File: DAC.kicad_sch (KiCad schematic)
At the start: 7 parts

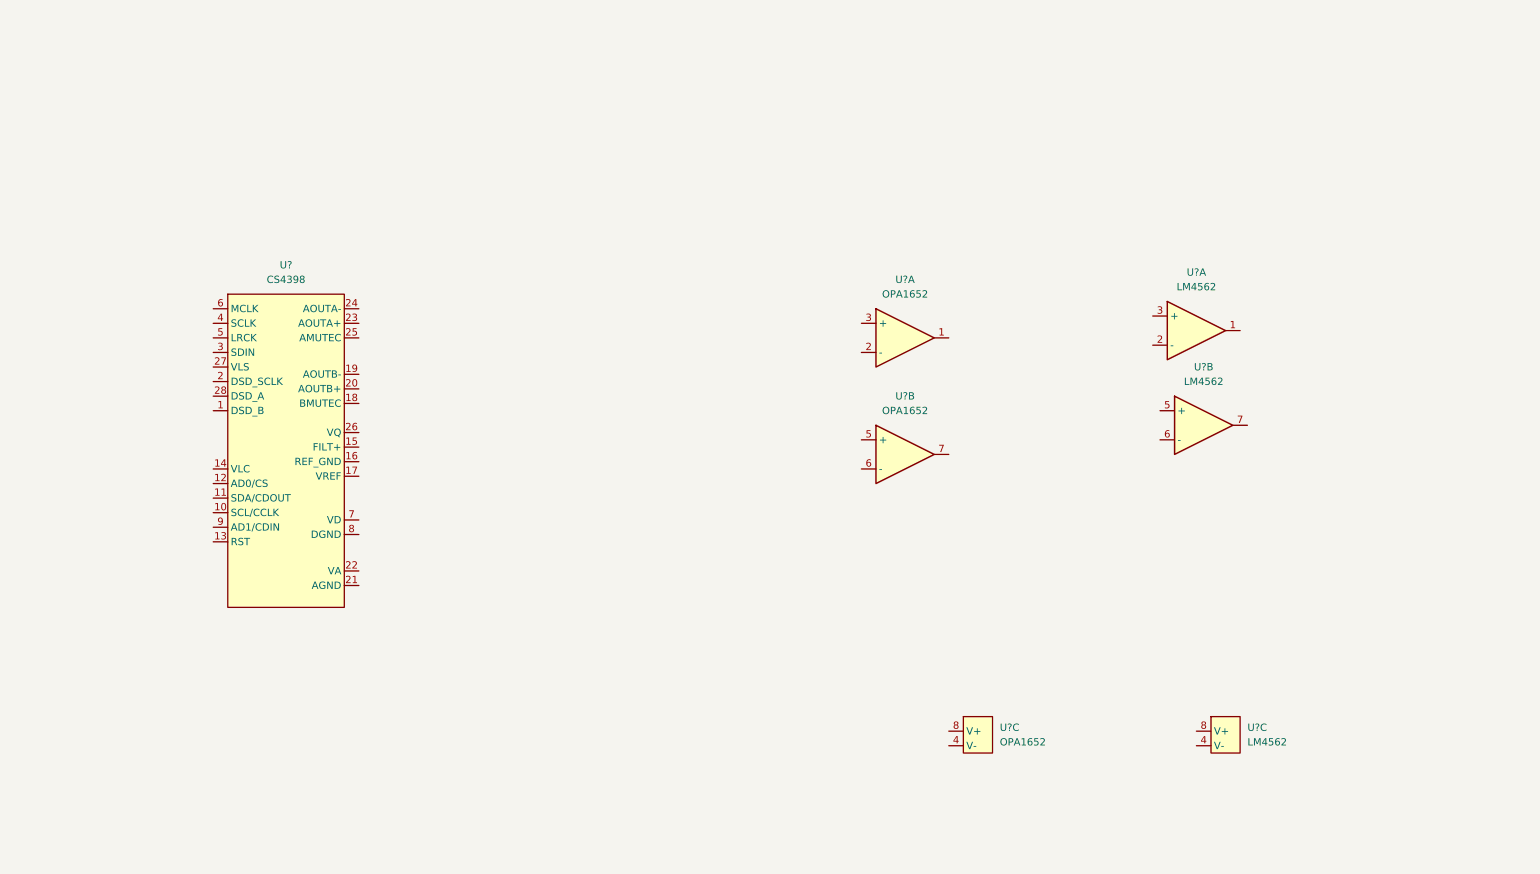
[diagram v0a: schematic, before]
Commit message: added SOC list
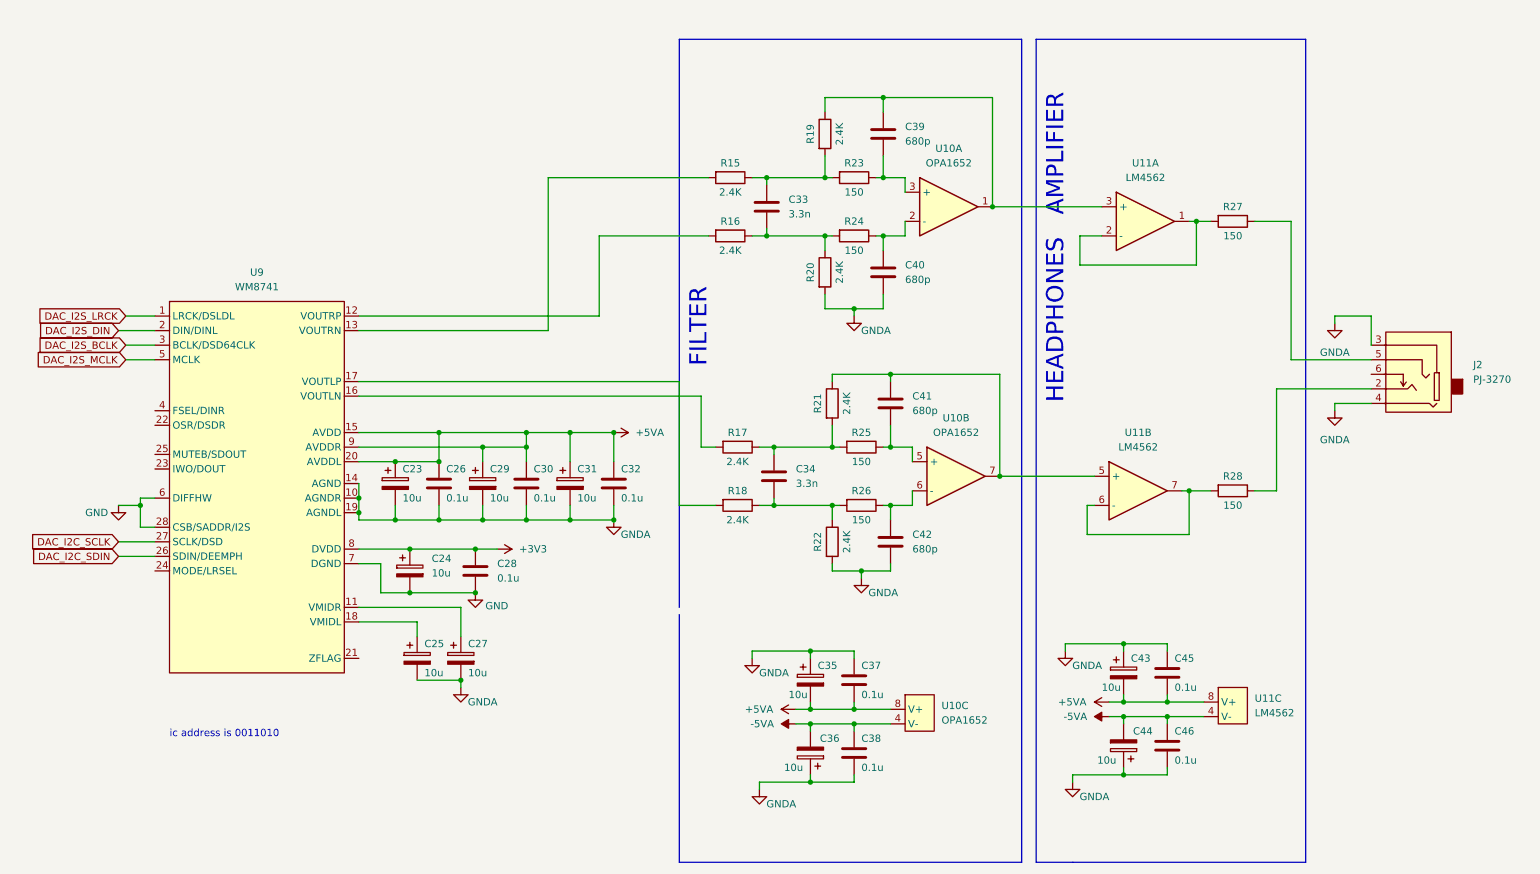
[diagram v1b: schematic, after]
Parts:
- removed U?: CS4398, Package_SO:TSSOP-28_6.1x9.7mm_P0.65mm, symbol rlib_ic:CS4398
- added C23, C24, C25, C27, C29, C31, C35, C36, C43, C44: 10u, symbol Device:C_Polarized
- added C26, C28, C30, C32, C37, C38, C45, C46: 0.1u, symbol Device:C
- added C33, C34: 3.3n, symbol Device:C
- added C39, C40, C41, C42: 680p, symbol Device:C
- added J2: PJ-3270, rlib_connectors:PJ-3270, symbol rlib_connectors:PJ-3270
- added R15, R16, R17, R18, R19, R20, R21, R22: 2.4K, symbol Device:R
- added R23, R24, R25, R26, R27, R28: 150, symbol Device:R
- added U9: WM8741, Package_SO:SSOP-28_5.3x10.2mm_P0.65mm, symbol rlib_ic:WM8741
- gave numbers to parts that had none: 2
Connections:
- net at U11.1: now also U11.2 (-), R27.2
- net at U11.3 (+): now also U10.1, C39.1, R19.1
- net at U10.2 (-): now also C40.1, R24.1
- net at U10.3 (+): now also C39.2, R23.1
- net at U10.5 (+): now also C41.2, R25.1
- net at U10.6 (-): now also C42.1, R26.1
- net at U10.7: now also U11.5 (+), C41.1, R21.1
- net -5VA: now reaches U10.4 (V-)
- net -5VA: now also U11.4 (V-), C36.2, C38.1, C44.2, C46.1
- net +5VA: now reaches U10.8 (V+)
- net +5VA: now also U11.8 (V+), C23.1, C26.1, C29.1, C30.1, C31.1, C32.1, C35.2, C37.2, C43.2, C45.2, U9.15 (AVDD), U9.20 (AVDDL), U9.9 (AVDDR)
- net at U11.6 (-): now also U11.7, R28.2
- new net: C34.1, R17.1, R21.2, R25.2
- new net: C34.2, R18.1, R22.1, R26.2
- new net: R17.2, U9.16 (VOUTLN)
- new net: J2.5, R27.1
- new net: J2.2, R28.1
- new net: C33.2, R16.1, R20.1, R24.2
- new net: C33.1, R15.1, R19.2, R23.2
- new net: C27.1, U9.11 (VMIDR)
- new net: R16.2, U9.12 (VOUTRP)
- new net: R15.2, U9.13 (VOUTRN)
- new net: R18.2, U9.17 (VOUTLP)
- new net: C25.1, U9.18 (VMIDL)
- new net +3V3: C24.1, C28.1, U9.8 (DVDD)
- new net DAC_I2C_SCLK: U9.27 (SCLK/DSD)
- new net DAC_I2C_SDIN: U9.26 (SDIN/DEEMPH)
- new net DAC_I2S_BCLK: U9.3 (BCLK/DSD64CLK)
- new net DAC_I2S_DIN: U9.2 (DIN/DINL)
- new net DAC_I2S_LRCK: U9.1 (LRCK/DSLDL)
- new net DAC_I2S_MCLK: U9.5 (MCLK)
- new net GND: C24.2, C28.2, U9.28 (CSB/SADDR/I2S), U9.6 (DIFFHW), U9.7 (DGND)
- new net GNDA: C23.2, C25.2, C26.2, C27.2, C29.2, C30.2, C31.2, C32.2, C35.1, C36.1, C37.1, C38.2, C40.2, C42.2, C43.1, C44.1, C45.1, C46.2, J2.3, J2.4, R20.2, R22.2, U9.10 (AGNDR), U9.14 (AGND), U9.19 (AGNDL)
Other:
- note added: "FILTER"
- note added: "HEADPHONES AMPLIFIER"
- note added: "ic address is 0011010"
- moved on the sheet: U10A, U10B, U10C, U11A, U11B, U11C

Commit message: dfdfasfasf
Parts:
- C23, C24, C25, C27, C29, C31, C35, C36, C43, C44: symbol Device:C_Polarized -> rlib_passive:C_Pol
- C26, C28, C30, C32, C33, C34, C37, C38, C39, C40, C41, C42, C45, C46: symbol Device:C -> rlib_passive:C
- R15, R16, R17, R18, R19, R20, R21, R22, R23, R24, R25, R26, R27, R28: symbol Device:R -> rlib_passive:R
- U10, U11: footprint Package_SO:SOIC-8_3.9x4.9mm_P1.27mm -> rlib_ic:SOIC-8_3.9x4.9mm_P1.27mm
- U9: footprint Package_SO:SSOP-28_5.3x10.2mm_P0.65mm -> rlib_ic:SSOP-28_5.3x10.2mm_P0.65mm

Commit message: lradc schematic
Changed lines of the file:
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@@
     (stroke (width 0) (type default) (color 0 0 0 1))
   )
-  (text "ic address is 0011010 " (at 38.1 137.16 0)
+  (text "ic address is 0011010 " (at 38.1 129.54 0)
     (effects (font (size 1.27 1.27)) (justify left bottom))
   )

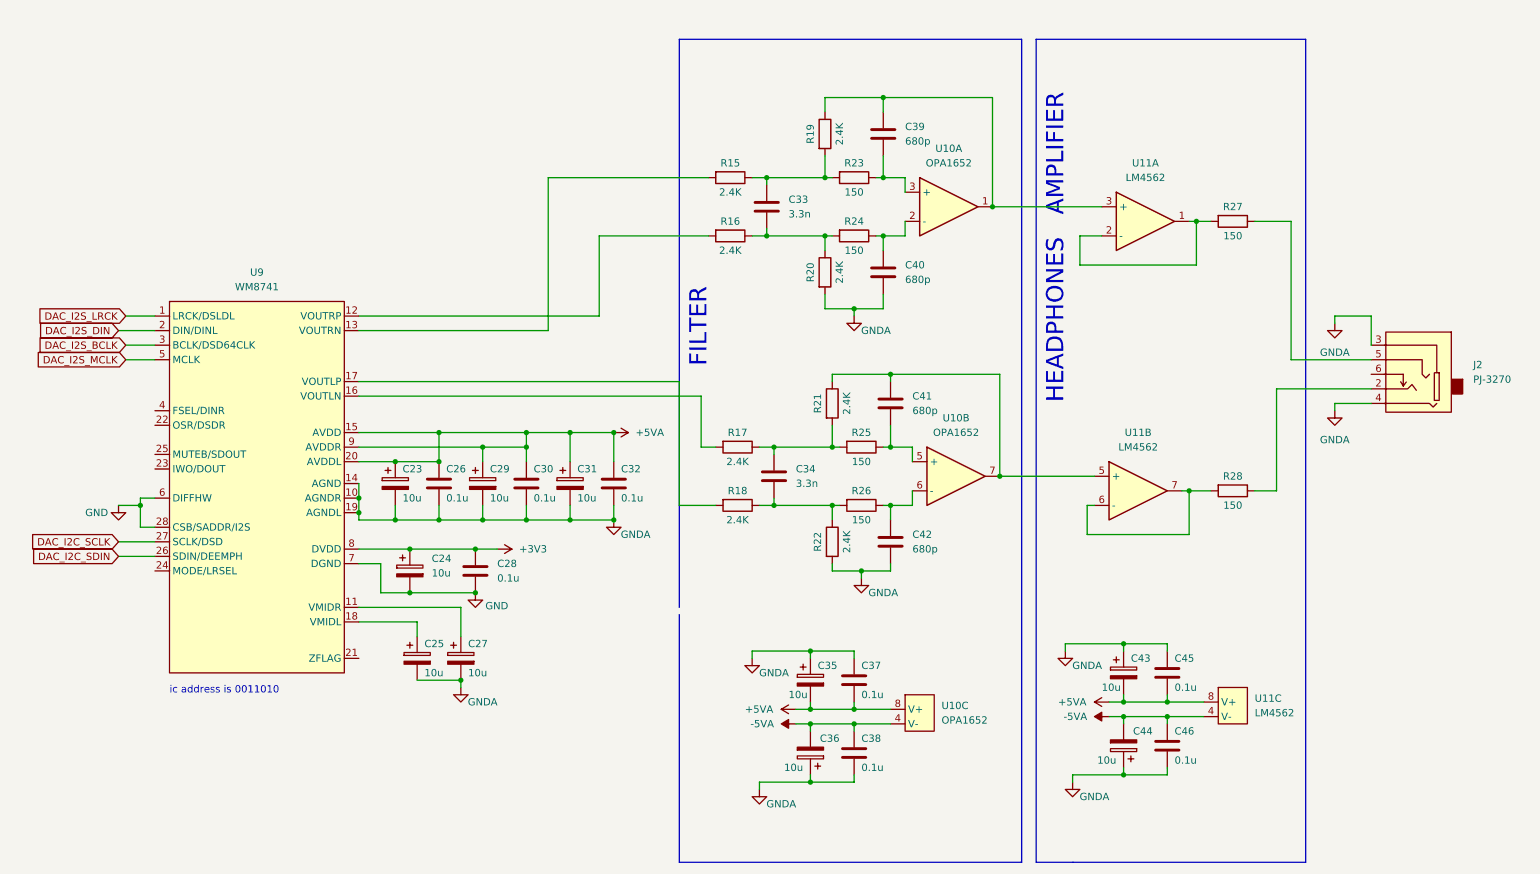
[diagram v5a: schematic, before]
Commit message: added crystal,backlight regulator and usb nets
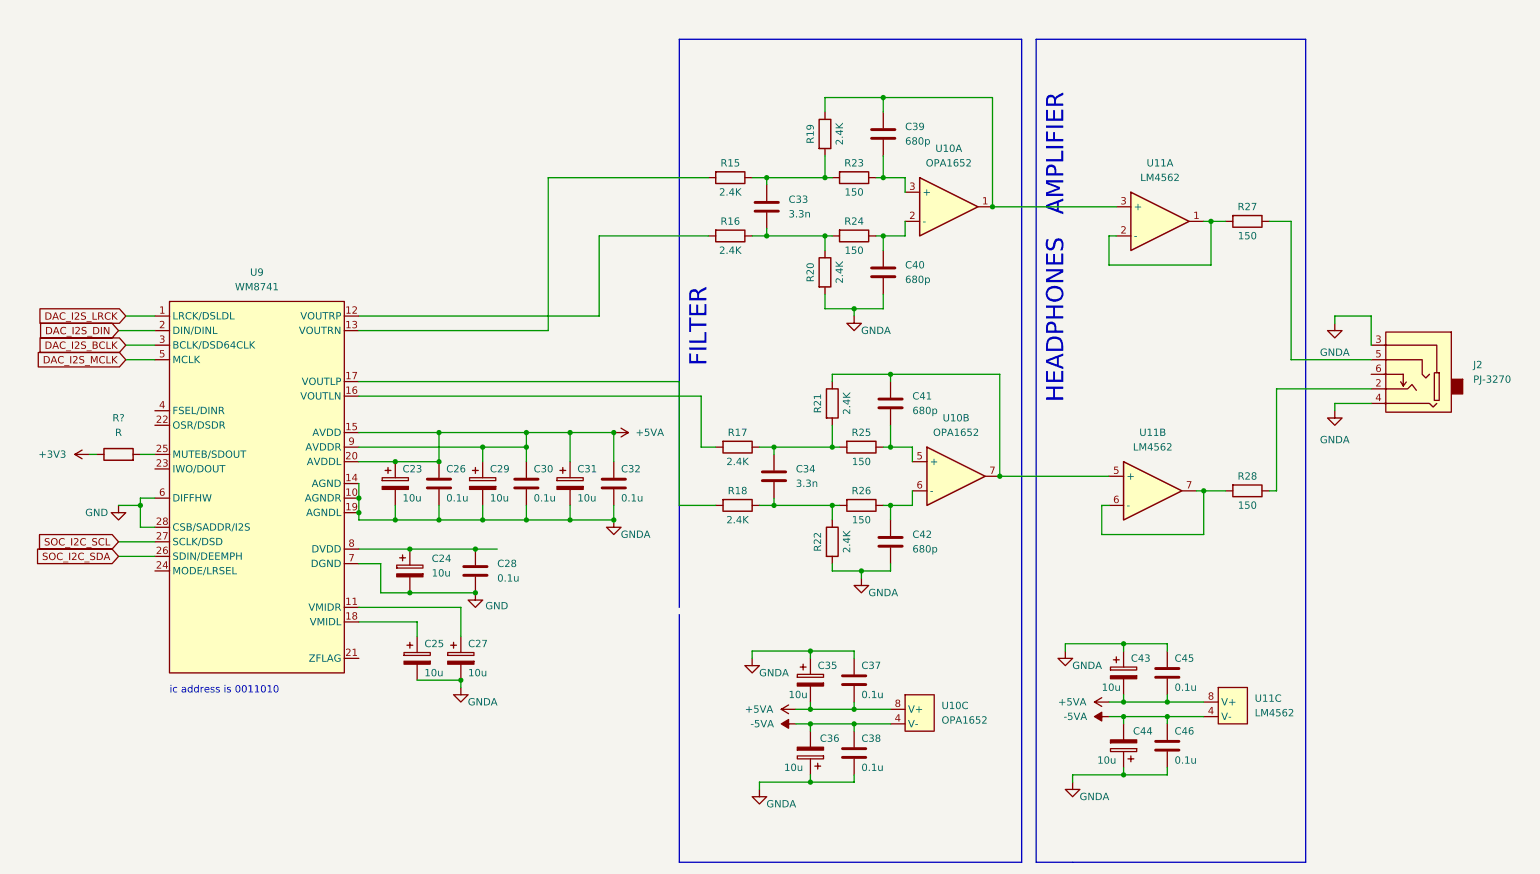
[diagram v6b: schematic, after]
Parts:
- added R?: R, symbol rlib_passive:R
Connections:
- net +3V3: now also R?.1; no longer C24.1, C28.1, U9.8 (DVDD)
- net at U9.25 (MUTEB/SDOUT): now also R?.2
- net DAC_I2C_SCLK renamed SOC_I2C_SCL
- net DAC_I2C_SDIN renamed SOC_I2C_SDA
- new net: C24.1, C28.1, U9.8 (DVDD)
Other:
- moved on the sheet: R27, R28, U11A, U11B

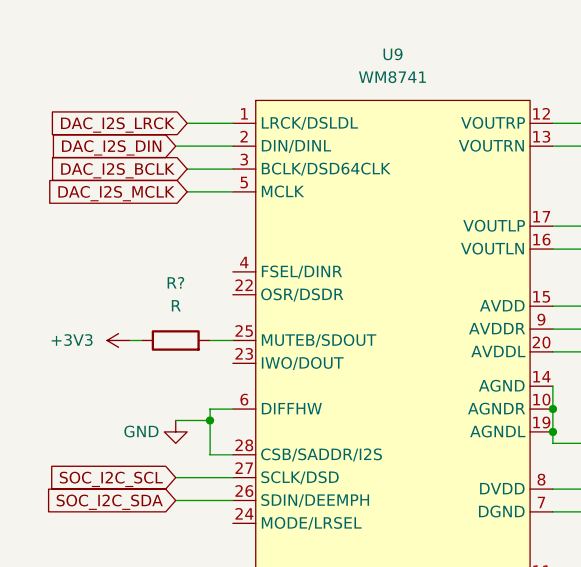
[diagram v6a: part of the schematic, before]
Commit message: changed volume buttons
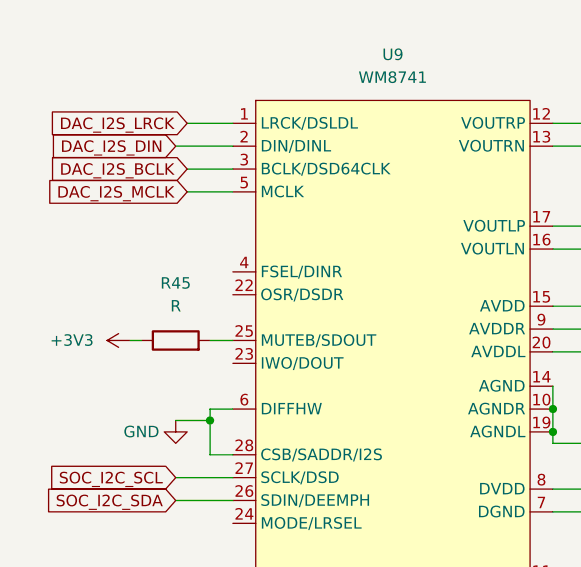
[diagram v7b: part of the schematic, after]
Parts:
- gave numbers to parts that had none: 1
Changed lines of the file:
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@@
   (symbol (lib_id "rlib_passive:R") (at 29.21 87.63 90) (unit 1)
     (in_bom yes) (on_board yes) (fields_autoplaced)
-    (property "Reference" "R?" (id 0) (at 29.21 81.28 90))
+    (property "Reference" "R45" (id 0) (at 29.21 81.28 90))
     (property "Value" "R" (id 1) (at 29.21 83.82 90))
     (property "Footprint" "" (id 2) (at 29.21 89.408 90)
@@
   (symbol (lib_id "power:+3V3") (at 24.13 87.63 90) (unit 1)
     (in_bom yes) (on_board yes)
-    (property "Reference" "#PWR?" (id 0) (at 27.94 87.63 0)
+    (property "Reference" "#PWR0140" (id 0) (at 27.94 87.63 0)
       (effects (font (size 1.27 1.27)) hide)
     )

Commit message: adde power source 3v0, molex connector, restistor footprints
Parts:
- R45: footprint (none) -> rlib_passive:R_0603_1608Metric
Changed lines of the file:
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@@
     (property "Reference" "R45" (id 0) (at 29.21 81.28 90))
     (property "Value" "R" (id 1) (at 29.21 83.82 90))
-    (property "Footprint" "" (id 2) (at 29.21 89.408 90)
+    (property "Footprint" "rlib_passive:R_0603_1608Metric" (id 2) (at 29.21 89.408 90)
       (effects (font (size 1.27 1.27)) hide)
     )
